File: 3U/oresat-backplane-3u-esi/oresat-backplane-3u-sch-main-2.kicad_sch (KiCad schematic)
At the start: 16 parts

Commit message: Added schematic and board variables, polished some silkscreen, reviewed board, renamed directory
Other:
- company: Portland State Aerospace Society -> PSAS / ESI
- title: Generic OreSat 3U Backplane -> OreSat 3U Backplane for ESI
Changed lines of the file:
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@@
 	(paper "B")
 	(title_block
-		(title "Generic OreSat 3U Backplane")
-		(date "2025-10-21")
+		(title "OreSat 3U Backplane for ESI")
+		(date "2026-02-20")
 		(rev "1.0")
-		(company "Portland State Aerospace Society")
+		(company "PSAS / ESI")
 	)
 	(text "SLOTS 14-17 UNUSED; ADCS FILL\n"

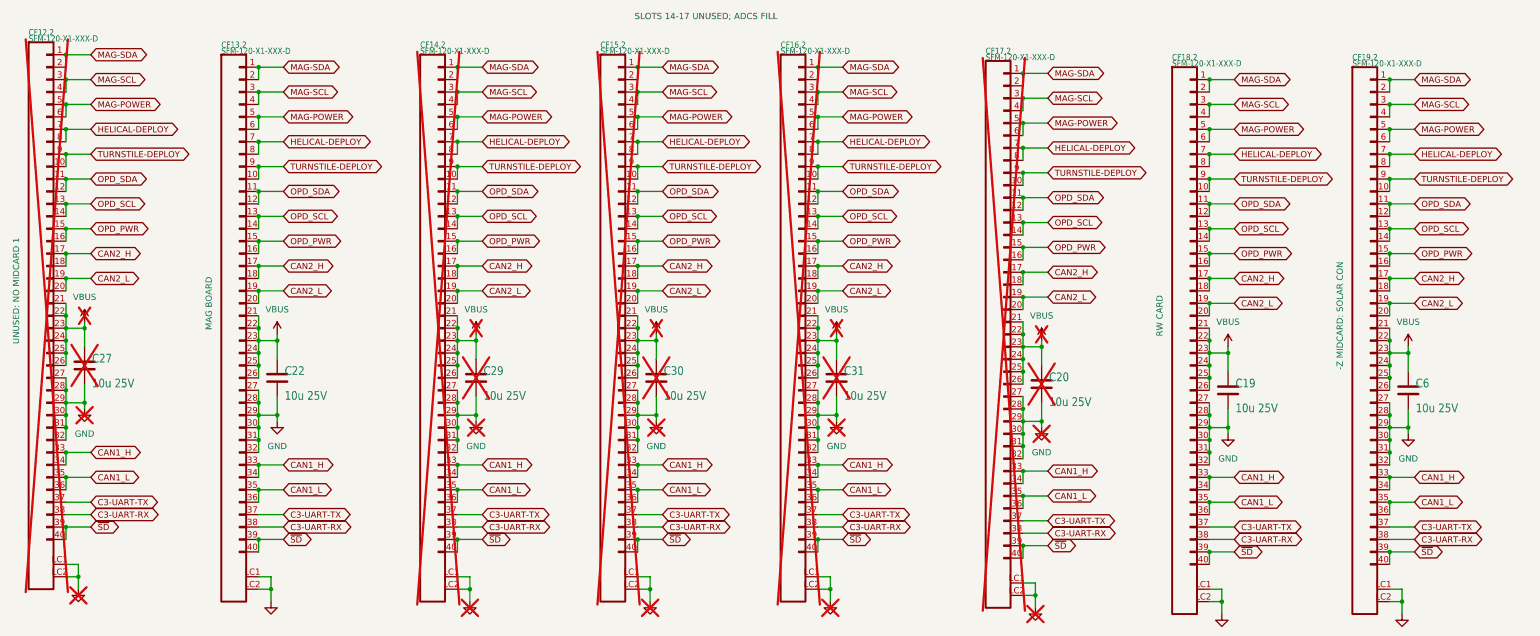
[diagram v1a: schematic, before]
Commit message: Labelled connectors & disconnected C3 LBand
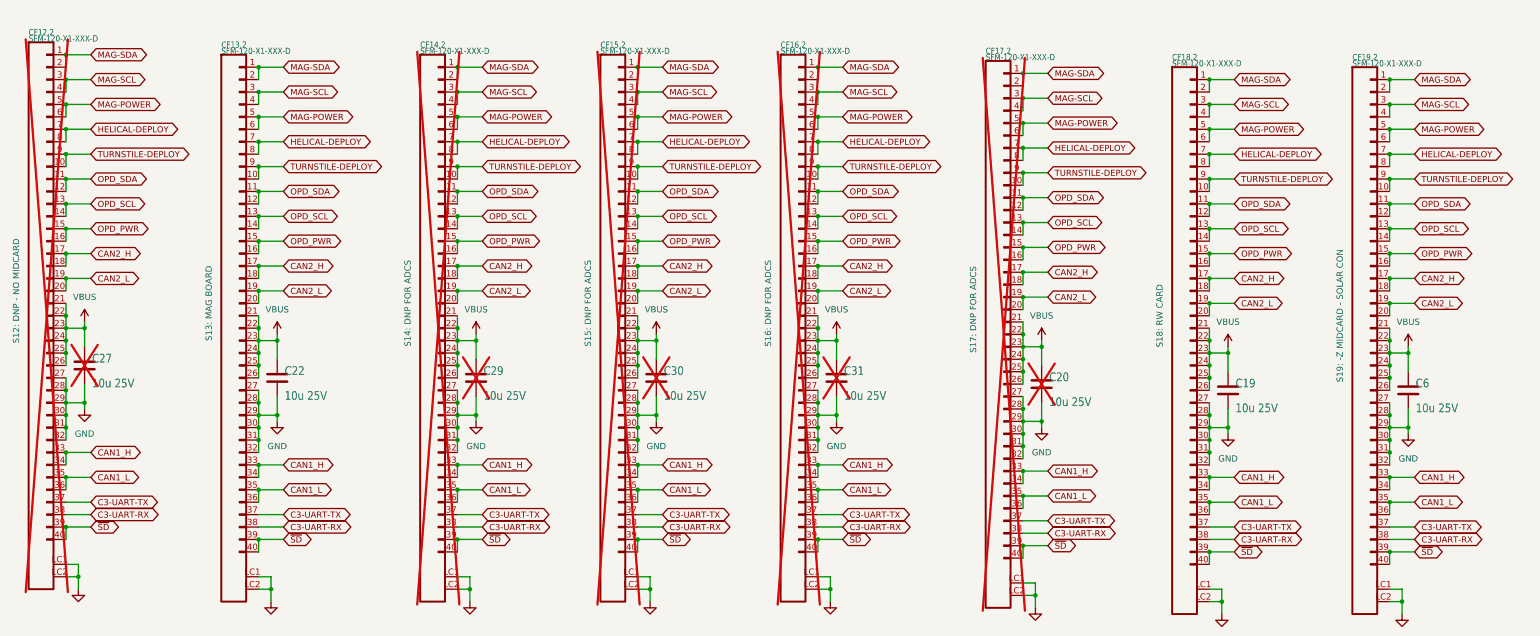
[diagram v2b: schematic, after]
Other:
- note removed: "SLOTS 14-17 UNUSED; ADCS FILL"
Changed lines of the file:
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@@
 		(company "PSAS / ESI")
 	)
-	(text "SLOTS 14-17 UNUSED; ADCS FILL\n"
-		(exclude_from_sim no)
-		(at 214.63 66.04 0)
-		(effects
-			(font
-				(size 1.27 1.27)
-			)
-		)
-	)
 	(junction
 		(at 123.19 172.72)
@@
 		(in_bom yes)
 		(on_board yes)
-		(dnp yes)
+		(dnp no)
 		(property "Reference" "#GND017"
 			(at 203.2 185.42 0)
@@
 			)
 		)
-		(property "Description" "UNUSED: NO MIDCARD 1"
+		(property "Description" "S12: DNP - NO MIDCARD"
 			(at 73.66 121.92 90)
 			(effects
@@
 			)
 		)
-		(property "Description" ""
-			(at 274.32 125.73 0)
+		(property "Description" "S17: DNP FOR ADCS"
+			(at 269.24 125.73 90)
 			(effects
 				(font
@@
 		(in_bom yes)
 		(on_board yes)
-		(dnp yes)
+		(dnp no)
 		(fields_autoplaced yes)
 		(property "Reference" "#PWR015"
@@
 		(in_bom yes)
 		(on_board yes)
-		(dnp yes)
+		(dnp no)
 		(fields_autoplaced yes)
 		(property "Reference" "#PWR014"
@@
 		(in_bom yes)
 		(on_board yes)
-		(dnp yes)
+		(dnp no)
 		(fields_autoplaced yes)
 		(property "Reference" "#VBUS015"
@@
 		(in_bom yes)
 		(on_board yes)
-		(dnp yes)
+		(dnp no)
 		(property "Reference" "#GND018"
 			(at 240.03 185.42 0)
@@
 		(in_bom yes)
 		(on_board yes)
-		(dnp yes)
+		(dnp no)
 		(fields_autoplaced yes)
 		(property "Reference" "#VBUS012"
@@
 			)
 		)
-		(property "Description" "-Z MIDCARD: SOLAR CON"
+		(property "Description" "S19: -Z MIDCARD - SOLAR CON"
 			(at 344.17 127 90)
 			(effects
@@
 		(in_bom yes)
 		(on_board yes)
-		(dnp yes)
+		(dnp no)
 		(property "Reference" "#GND016"
 			(at 166.37 185.42 0)
@@
 			)
 		)
-		(property "Description" ""
-			(at 232.41 124.46 0)
+		(property "Description" "S16: DNP FOR ADCS"
+			(at 227.33 124.46 90)
 			(effects
 				(font
@@
 		(in_bom yes)
 		(on_board yes)
-		(dnp yes)
+		(dnp no)
 		(fields_autoplaced yes)
 		(property "Reference" "#VBUS016"
@@
 			)
 		)
-		(property "Description" "MAG BOARD"
+		(property "Description" "S13: MAG BOARD"
 			(at 113.03 124.46 90)
 			(effects
@@
 			)
 		)
-		(property "Description" ""
-			(at 158.75 124.46 0)
+		(property "Description" "S14: DNP FOR ADCS"
+			(at 153.67 124.46 90)
 			(effects
 				(font
@@
 		(in_bom yes)
 		(on_board yes)
-		(dnp yes)
+		(dnp no)
 		(fields_autoplaced yes)
 		(property "Reference" "#PWR012"
@@
 		(in_bom yes)
 		(on_board yes)
-		(dnp yes)
+		(dnp no)
 		(property "Reference" "#GND010"
 			(at 86.36 182.88 0)
@@
 			)
 		)
-		(property "Description" ""
-			(at 195.58 124.46 0)
+		(property "Description" "S15: DNP FOR ADCS"
+			(at 190.5 124.46 90)
 			(effects
 				(font
@@
 		(in_bom yes)
 		(on_board yes)
-		(dnp yes)
+		(dnp no)
 		(fields_autoplaced yes)
 		(property "Reference" "#PWR013"
@@
 		(in_bom yes)
 		(on_board yes)
-		(dnp yes)
+		(dnp no)
 		(fields_autoplaced yes)
 		(property "Reference" "#PWR017"
@@
 		(in_bom yes)
 		(on_board yes)
-		(dnp yes)
+		(dnp no)
 		(property "Reference" "#GND0111"
 			(at 281.94 186.69 0)
@@
 		(in_bom yes)
 		(on_board yes)
-		(dnp yes)
+		(dnp no)
 		(fields_autoplaced yes)
 		(property "Reference" "#VBUS017"
@@
 			)
 		)
-		(property "Description" "RW CARD"
+		(property "Description" "S18: RW CARD"
 			(at 307.34 127 90)
 			(effects
@@
 		(in_bom yes)
 		(on_board yes)
-		(dnp yes)
+		(dnp no)
 		(fields_autoplaced yes)
 		(property "Reference" "#VBUS014"

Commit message: Polish of 3U for ESI
Fixed ERC/DRC/sync errors. Made fancy RF table. Fixed BOM.
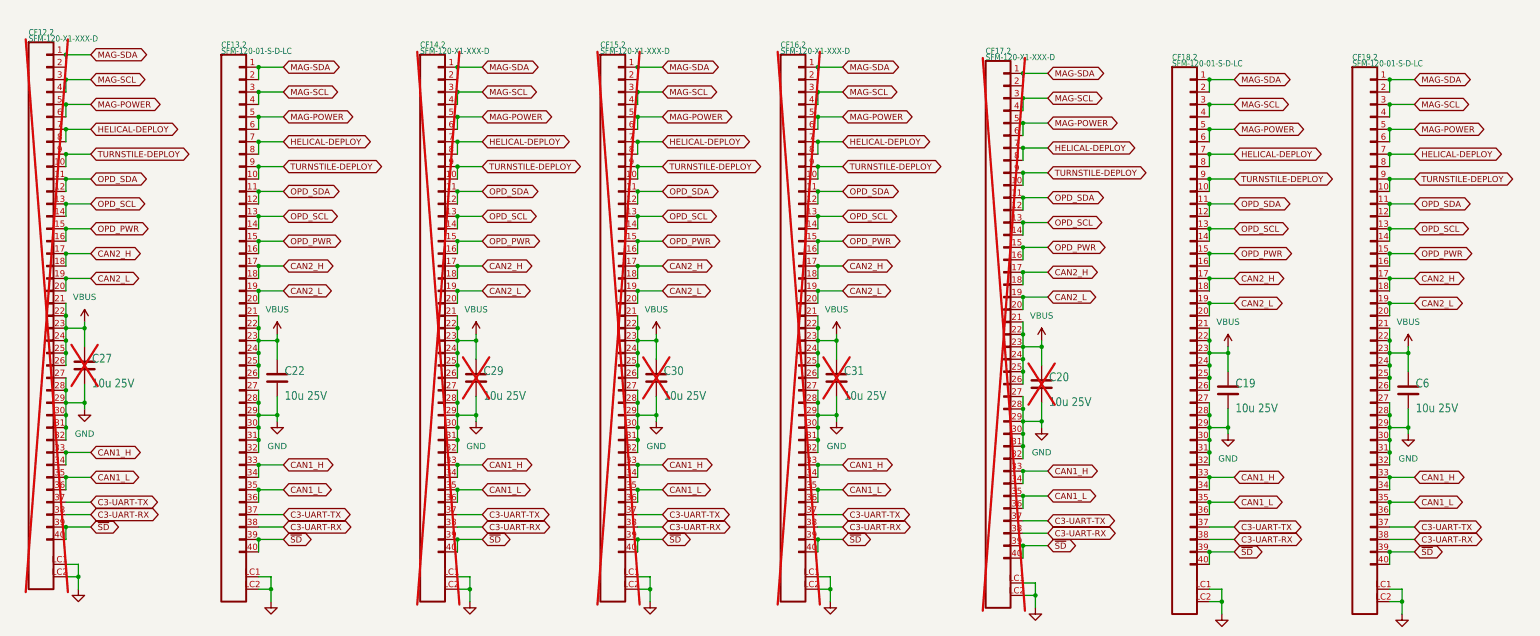
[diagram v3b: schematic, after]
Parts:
- C19, C20, C22, C27, C29, C30, C31, C6: DIS (none) -> DigiKey; DPN (none) -> 587-3485-1-ND; MFR (none) -> Taiyo Yuden; MPN (none) -> TMK316AB7106KLHT
- CF12.2, CF14.2, CF15.2, CF16.2, CF17.2: DIS (none) -> DigiKey; DPN (none) -> SAM11706-ND; MFR (none) -> Samtec Inc.; MPN (none) -> SFM-120-01-S-D-LC
- CF13.2, CF18.2, CF19.2: value SFM-120-X1-XXX-D -> SFM-120-01-S-D-LC; DIS (none) -> DigiKey; DPN (none) -> SAM11706-ND; MFR (none) -> Samtec Inc.; MPN (none) -> SFM-120-01-S-D-LC
